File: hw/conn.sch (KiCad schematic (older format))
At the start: 8 parts

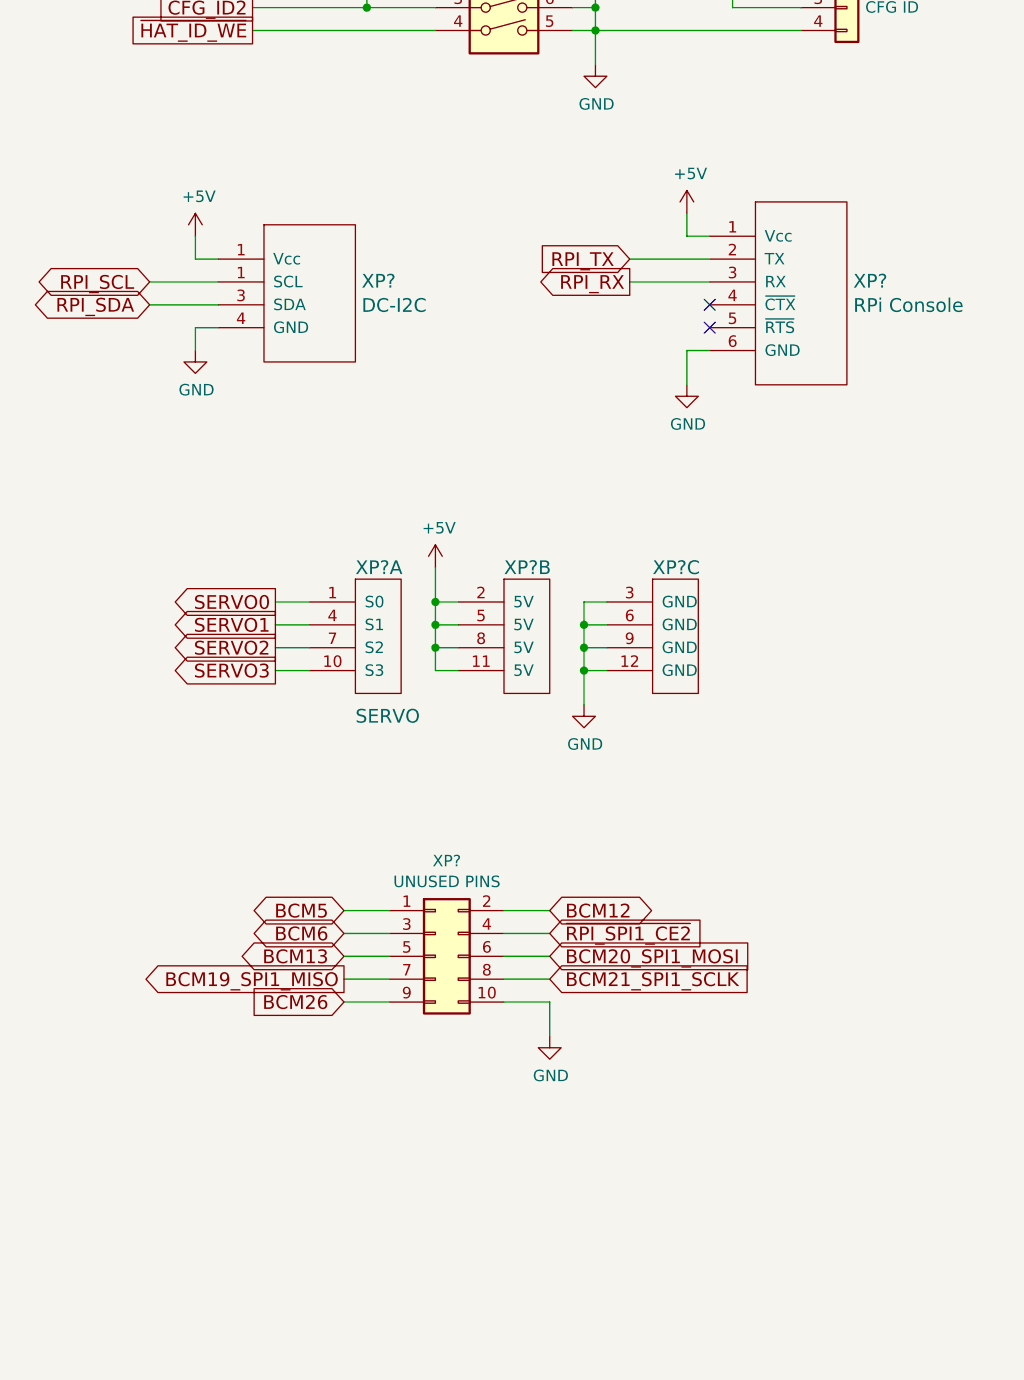
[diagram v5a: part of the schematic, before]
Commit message: hw: replace STM console and SWD with one connector. Rpi I2C and UART to DroneCode GPS port
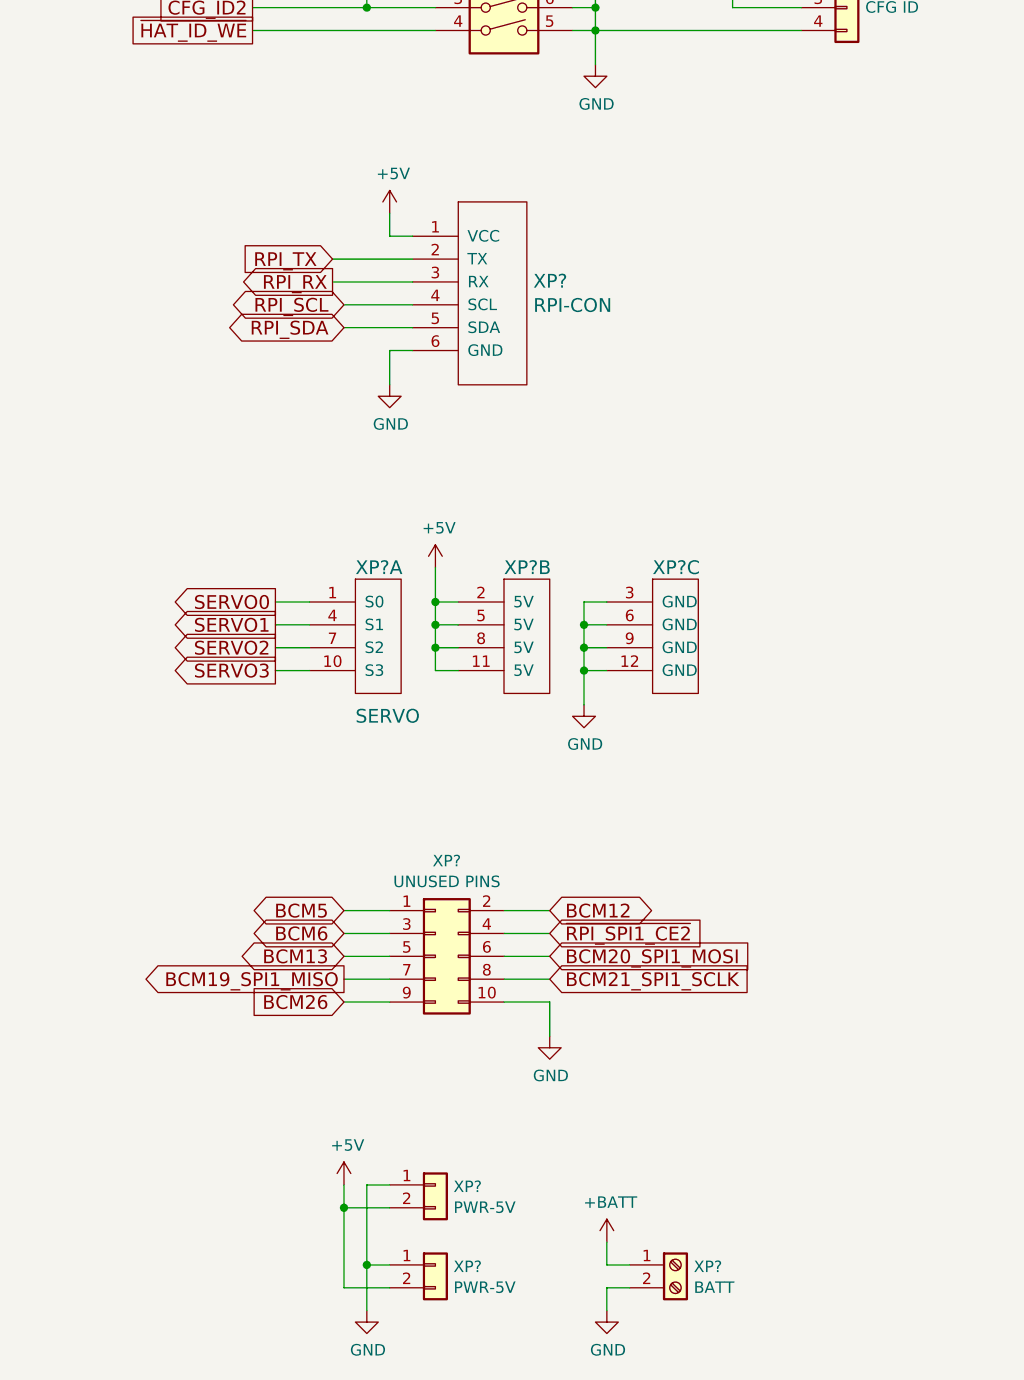
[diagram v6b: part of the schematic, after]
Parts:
- removed XP?: DC-I2C, symbol dronecode-conn:DC-I2C
- removed XP?: RPi Console, symbol dronecode-conn:DC-Telemetry
- added XP? (x2): PWR-5V, symbol Connector_Generic:Conn_01x02
- added XP?: BATT, symbol Connector_Specialized:Screw_Terminal_01x02
- added XP?: RPI-CON, symbol dronecode-conn:DC-GPS
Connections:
- net +5V: now also XP?.1 (VCC), XP?.2 (Pin_2), XP?.2 (Pin_2)
- net GND: now also XP?.1 (Pin_1), XP?.1 (Pin_1), XP?.2 (Pin_2), XP?.6 (GND)
- net RPI_RX: now also XP?.3 (RX)
- net RPI_SCL: now also XP?.4 (SCL)
- net RPI_SDA: now also XP?.5 (SDA)
- net RPI_TX: now also XP?.2 (TX)
- new net +BATT: XP?.1 (Pin_1)
- no-connect marks 2 -> 0
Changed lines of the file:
@@
 Wire Wire Line
 	3150 3150 3650 3150
-Text GLabel 4800 4250 0    60   Input ~ 0
+Text GLabel 3500 4250 0    60   Input ~ 0
 RPI_TX
-Text GLabel 4800 4350 0    60   Output ~ 0
+Text GLabel 3500 4350 0    60   Output ~ 0
 RPI_RX
 Text GLabel 4450 7300 2    60   Input ~ 0
@@
 Text GLabel 4450 7100 2    60   BiDi ~ 0
 BCM12
-Text GLabel 2700 4350 0    60   BiDi ~ 0
+Text GLabel 3550 4450 0    60   BiDi ~ 0
 RPI_SCL
-Text GLabel 2700 4450 0    60   BiDi ~ 0
+Text GLabel 3550 4550 0    60   BiDi ~ 0
 RPI_SDA
 Text GLabel 3550 7400 0    60   Output ~ 0
@@
 Text GLabel 3550 7200 0    60   BiDi ~ 0
 BCM6
-$Comp
-L dronecode-conn:DC-I2C XP?
-U 1 1 5AC44595
-P 3400 4400
-F 0 "XP?" H 3627 4453 60  0000 L CNN
-F 1 "DC-I2C" H 3627 4347 60  0000 L CNN
-F 2 "" H 3400 4400 60  0001 C CNN
-F 3 "https://wiki.dronecode.org/workgroup/connectors/start" H 3400 4400 60  0001 C CNN
-	1    3400 4400
-	1    0    0    -1
-$EndComp
-Wire Wire Line
-	2700 4350 3000 4350
-Wire Wire Line
-	2700 4450 3000 4450
-$Comp
-L power:GND #PWR?
-U 1 1 5AC44B9B
-P 2900 4650
-F 0 "#PWR?" H 2900 4400 50  0001 C CNN
-F 1 "GND" H 2905 4477 50  0000 C CNN
-F 2 "" H 2900 4650 50  0001 C CNN
-F 3 "" H 2900 4650 50  0001 C CNN
-	1    2900 4650
-	1    0    0    -1
-$EndComp
-$Comp
-L power:+5V #PWR?
-U 1 1 5AC44BF4
-P 2900 4150
-F 0 "#PWR?" H 2900 4000 50  0001 C CNN
-F 1 "+5V" H 2915 4323 50  0000 C CNN
-F 2 "" H 2900 4150 50  0001 C CNN
-F 3 "" H 2900 4150 50  0001 C CNN
-	1    2900 4150
-	1    0    0    -1
-$EndComp
-Wire Wire Line
-	3000 4250 2900 4250
-Wire Wire Line
-	2900 4250 2900 4150
-Wire Wire Line
-	2900 4650 2900 4550
-Wire Wire Line
-	2900 4550 3000 4550
+Wire Wire Line
+	3550 4450 3850 4450
+Wire Wire Line
+	3550 4550 3850 4550
 Text GLabel 3250 5750 0    60   Output ~ 0
 SERVO0
@@
 	5550 3250 4650 3250
 $Comp
-L dronecode-conn:DC-Telemetry XP?
-U 1 1 5AE1F895
-P 5550 4400
-F 0 "XP?" H 5778 4453 60  0000 L CNN
-F 1 "RPi Console" H 5778 4347 60  0000 L CNN
-F 2 "" H 5550 4400 60  0001 C CNN
-F 3 "https://wiki.dronecode.org/workgroup/connectors/start" H 5550 4400 60  0001 C CNN
-	1    5550 4400
-	1    0    0    -1
-$EndComp
-$Comp
 L power:GND #PWR?
 U 1 1 5AE1FA9F
-P 5050 4800
-F 0 "#PWR?" H 5050 4550 50  0001 C CNN
-F 1 "GND" H 5055 4627 50  0000 C CNN
-F 2 "" H 5050 4800 50  0001 C CNN
-F 3 "" H 5050 4800 50  0001 C CNN
-	1    5050 4800
+P 3750 4800
+F 0 "#PWR?" H 3750 4550 50  0001 C CNN
+F 1 "GND" H 3755 4627 50  0000 C CNN
+F 2 "" H 3750 4800 50  0001 C CNN
+F 3 "" H 3750 4800 50  0001 C CNN
+	1    3750 4800
 	1    0    0    -1
 $EndComp
@@
 L power:+5V #PWR?
 U 1 1 5AE1FAB8
-P 5050 4050
-F 0 "#PWR?" H 5050 3900 50  0001 C CNN
-F 1 "+5V" H 5065 4223 50  0000 C CNN
-F 2 "" H 5050 4050 50  0001 C CNN
-F 3 "" H 5050 4050 50  0001 C CNN
-	1    5050 4050
-	1    0    0    -1
-$EndComp
-Wire Wire Line
-	4800 4250 5150 4250
-Wire Wire Line
-	5150 4350 4800 4350
-Wire Wire Line
-	5150 4150 5050 4150
-Wire Wire Line
-	5050 4150 5050 4050
-Wire Wire Line
-	5150 4650 5050 4650
-Wire Wire Line
-	5050 4650 5050 4800
-NoConn ~ 5150 4550
-NoConn ~ 5150 4450
+P 3750 4050
+F 0 "#PWR?" H 3750 3900 50  0001 C CNN
+F 1 "+5V" H 3765 4223 50  0000 C CNN
+F 2 "" H 3750 4050 50  0001 C CNN
+F 3 "" H 3750 4050 50  0001 C CNN
+	1    3750 4050
+	1    0    0    -1
+$EndComp
+Wire Wire Line
+	3500 4250 3850 4250
+Wire Wire Line
+	3850 4350 3500 4350
+Wire Wire Line
+	3850 4150 3750 4150
+Wire Wire Line
+	3750 4150 3750 4050
+Wire Wire Line
+	3850 4650 3750 4650
+Wire Wire Line
+	3750 4650 3750 4800
 $Comp
 L Connector_Generic:Conn_02x05_Odd_Even XP?
@@
 Wire Wire Line
 	4450 7500 4450 7650
+$Comp
+L Connector_Generic:Conn_01x02 XP?
+U 1 1 5ADAC8B3
+P 3950 8300
+F 0 "XP?" H 4029 8292 50  0000 L CNN
+F 1 "PWR-5V" H 4029 8201 50  0000 L CNN
+F 2 "" H 3950 8300 50  0001 C CNN
+F 3 "~" H 3950 8300 50  0001 C CNN
+	1    3950 8300
+	1    0    0    -1
+$EndComp
+$Comp
+L Connector_Generic:Conn_01x02 XP?
+U 1 1 5ADACAD0
+P 3950 8650
+F 0 "XP?" H 4029 8642 50  0000 L CNN
+F 1 "PWR-5V" H 4029 8551 50  0000 L CNN
+F 2 "" H 3950 8650 50  0001 C CNN
+F 3 "~" H 3950 8650 50  0001 C CNN
+	1    3950 8650
+	1    0    0    -1
+$EndComp
+$Comp
+L power:GND #PWR?
+U 1 1 5ADAE6E2
+P 3650 8850
+F 0 "#PWR?" H 3650 8600 50  0001 C CNN
+F 1 "GND" H 3655 8677 50  0000 C CNN
+F 2 "" H 3650 8850 50  0001 C CNN
+F 3 "" H 3650 8850 50  0001 C CNN
+	1    3650 8850
+	1    0    0    -1
+$EndComp
+$Comp
+L power:+5V #PWR?
+U 1 1 5ADAEA7B
+P 3550 8300
+F 0 "#PWR?" H 3550 8150 50  0001 C CNN
+F 1 "+5V" H 3565 8473 50  0000 C CNN
+F 2 "" H 3550 8300 50  0001 C CNN
+F 3 "" H 3550 8300 50  0001 C CNN
+	1    3550 8300
+	1    0    0    -1
+$EndComp
+Wire Wire Line
+	3750 8300 3650 8300
+Wire Wire Line
+	3650 8300 3650 8650
+Wire Wire Line
+	3650 8650 3750 8650
+Connection ~ 3650 8650
+Wire Wire Line
+	3650 8650 3650 8850
+Wire Wire Line
+	3750 8750 3550 8750
+Wire Wire Line
+	3550 8750 3550 8400
+Wire Wire Line
+	3750 8400 3550 8400
+Connection ~ 3550 8400
+Wire Wire Line
+	3550 8400 3550 8300
+$Comp
+L Connector_Specialized:Screw_Terminal_01x02 XP?
+U 1 1 5ADC296E
+P 5000 8650
+F 0 "XP?" H 5080 8642 50  0000 L CNN
+F 1 "BATT" H 5080 8551 50  0000 L CNN
+F 2 "" H 5000 8650 50  0001 C CNN
+F 3 "~" H 5000 8650 50  0001 C CNN
+	1    5000 8650
+	1    0    0    -1
+$EndComp
+$Comp
+L power:GND #PWR?
+U 1 1 5ADC2D33
+P 4700 8850
+F 0 "#PWR?" H 4700 8600 50  0001 C CNN
+F 1 "GND" H 4705 8677 50  0000 C CNN
+F 2 "" H 4700 8850 50  0001 C CNN
+F 3 "" H 4700 8850 50  0001 C CNN
+	1    4700 8850
+	1    0    0    -1
+$EndComp
+$Comp
+L power:+BATT #PWR?
+U 1 1 5ADC2DB8
+P 4700 8550
+F 0 "#PWR?" H 4700 8400 50  0001 C CNN
+F 1 "+BATT" H 4715 8723 50  0000 C CNN
+F 2 "" H 4700 8550 50  0001 C CNN
+F 3 "" H 4700 8550 50  0001 C CNN
+	1    4700 8550
+	1    0    0    -1
+$EndComp
+Wire Wire Line
+	4800 8650 4700 8650
+Wire Wire Line
+	4700 8650 4700 8550
+Wire Wire Line
+	4800 8750 4700 8750
+Wire Wire Line
+	4700 8750 4700 8850
+$Comp
+L dronecode-conn:DC-GPS XP?
+U 1 1 5AE4627A
+P 4200 4400
+F 0 "XP?" H 4378 4453 60  0000 L CNN
+F 1 "RPI-CON" H 4378 4347 60  0000 L CNN
+F 2 "" H 4150 4400 60  0001 C CNN
+F 3 "" H 4150 4400 60  0001 C CNN
+	1    4200 4400
+	1    0    0    -1
+$EndComp
 $EndSCHEMATC

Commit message: hw: sch ready
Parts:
- gave numbers to parts that had none: 9
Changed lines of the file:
@@
 $EndDescr
 $Comp
-L Switch:SW_DIP_x04 SW?
+L Switch:SW_DIP_x04 SW1
 U 1 1 5AC0CE65
 P 4250 3150
-F 0 "SW?" H 4250 3617 50  0000 C CNN
+F 0 "SW1" H 4250 3617 50  0000 C CNN
 F 1 "SW_DIP_x04" H 4250 3526 50  0000 C CNN
 F 2 "" H 4250 3150 50  0001 C CNN
@@
 	3150 3050 3550 3050
 $Comp
-L power:GND #PWR?
+L power:GND #PWR049
 U 1 1 5AC0D0C3
 P 4650 3400
-F 0 "#PWR?" H 4650 3150 50  0001 C CNN
+F 0 "#PWR049" H 4650 3150 50  0001 C CNN
 F 1 "GND" H 4655 3227 50  0000 C CNN
 F 2 "" H 4650 3400 50  0001 C CNN
@@
 SERVO3
 $Comp
-L dronecode-conn:Servo-Conn4 XP?
+L dronecode-conn:Servo-Conn4 XP10
 U 1 1 5AE13059
 P 3700 5900
-F 0 "XP?" H 3600 6200 60  0000 L CNN
+F 0 "XP10" H 3600 6200 60  0000 L CNN
 F 1 "SERVO" H 3600 5550 60  0000 L CNN
 F 2 "" H 3650 5900 60  0001 C CNN
@@
 $EndComp
 $Comp
-L dronecode-conn:Servo-Conn4 XP?
+L dronecode-conn:Servo-Conn4 XP11
 U 2 1 5AE130D9
 P 4350 5900
-F 0 "XP?" H 4250 6200 60  0000 L CNN
+F 0 "XP11" H 4250 6200 60  0000 L CNN
 F 1 "Servo-Conn4" H 4477 5847 60  0001 L CNN
 F 2 "" H 4300 5900 60  0001 C CNN
@@
 $EndComp
 $Comp
-L dronecode-conn:Servo-Conn4 XP?
+L dronecode-conn:Servo-Conn4 XP11
 U 3 1 5AE13114
 P 5000 5900
-F 0 "XP?" H 4900 6200 60  0000 L CNN
+F 0 "XP11" H 4900 6200 60  0000 L CNN
 F 1 "Servo-Conn4" H 5127 5847 60  0001 L CNN
 F 2 "" H 4950 5900 60  0001 C CNN
@@
 	3250 6050 3400 6050
 $Comp
-L power:GND #PWR?
+L power:GND #PWR053
 U 1 1 5AE14A11
 P 4600 6200
-F 0 "#PWR?" H 4600 5950 50  0001 C CNN
+F 0 "#PWR053" H 4600 5950 50  0001 C CNN
 F 1 "GND" H 4605 6027 50  0000 C CNN
 F 2 "" H 4600 6200 50  0001 C CNN
@@
 $EndComp
 $Comp
-L power:+5V #PWR?
+L power:+5V #PWR052
 U 1 1 5AE14A3F
 P 3950 5600
-F 0 "#PWR?" H 3950 5450 50  0001 C CNN
+F 0 "#PWR052" H 3950 5450 50  0001 C CNN
 F 1 "+5V" H 3965 5773 50  0000 C CNN
 F 2 "" H 3950 5600 50  0001 C CNN
@@
 	4600 6050 4600 6200
 $Comp
-L Connector_Generic:Conn_01x04 XP?
+L Connector_Generic:Conn_01x04 XP8
 U 1 1 5AE192BA
 P 5750 3050
-F 0 "XP?" H 5830 3042 50  0000 L CNN
+F 0 "XP8" H 5830 3042 50  0000 L CNN
 F 1 "CFG ID" H 5830 2951 50  0000 L CNN
 F 2 "" H 5750 3050 50  0001 C CNN
@@
 	5550 3250 4650 3250
 $Comp
-L power:GND #PWR?
+L power:GND #PWR051
 U 1 1 5AE1FA9F
 P 3750 4800
-F 0 "#PWR?" H 3750 4550 50  0001 C CNN
+F 0 "#PWR051" H 3750 4550 50  0001 C CNN
 F 1 "GND" H 3755 4627 50  0000 C CNN
 F 2 "" H 3750 4800 50  0001 C CNN
@@
 $EndComp
 $Comp
-L power:+5V #PWR?
+L power:+5V #PWR050
 U 1 1 5AE1FAB8
 P 3750 4050
-F 0 "#PWR?" H 3750 3900 50  0001 C CNN
+F 0 "#PWR050" H 3750 3900 50  0001 C CNN
 F 1 "+5V" H 3765 4223 50  0000 C CNN
 F 2 "" H 3750 4050 50  0001 C CNN
@@
 	3750 4650 3750 4800
 $Comp
-L Connector_Generic:Conn_02x05_Odd_Even XP?
+L Connector_Generic:Conn_02x05_Odd_Even XP12
 U 1 1 5AE27376
 P 3950 7300
-F 0 "XP?" H 4000 7717 50  0000 C CNN
+F 0 "XP12" H 4000 7717 50  0000 C CNN
 F 1 "UNUSED PINS" H 4000 7626 50  0000 C CNN
 F 2 "" H 3950 7300 50  0001 C CNN
@@
 $EndComp
 $Comp
-L power:GND #PWR?
+L power:GND #PWR054
 U 1 1 5AE2781B
 P 4450 7650
-F 0 "#PWR?" H 4450 7400 50  0001 C CNN
+F 0 "#PWR054" H 4450 7400 50  0001 C CNN
 F 1 "GND" H 4455 7477 50  0000 C CNN
 F 2 "" H 4450 7650 50  0001 C CNN
@@
 	4450 7500 4450 7650
 $Comp
-L Connector_Generic:Conn_01x02 XP?
+L Connector_Generic:Conn_01x02 XP13
 U 1 1 5ADAC8B3
 P 3950 8300
-F 0 "XP?" H 4029 8292 50  0000 L CNN
+F 0 "XP13" H 4029 8292 50  0000 L CNN
 F 1 "PWR-5V" H 4029 8201 50  0000 L CNN
 F 2 "" H 3950 8300 50  0001 C CNN
@@
 $EndComp
 $Comp
-L Connector_Generic:Conn_01x02 XP?
+L Connector_Generic:Conn_01x02 XP14
 U 1 1 5ADACAD0
 P 3950 8650
-F 0 "XP?" H 4029 8642 50  0000 L CNN
+F 0 "XP14" H 4029 8642 50  0000 L CNN
 F 1 "PWR-5V" H 4029 8551 50  0000 L CNN
 F 2 "" H 3950 8650 50  0001 C CNN
@@
 $EndComp
 $Comp
-L power:GND #PWR?
+L power:GND #PWR057
 U 1 1 5ADAE6E2
 P 3650 8850
-F 0 "#PWR?" H 3650 8600 50  0001 C CNN
+F 0 "#PWR057" H 3650 8600 50  0001 C CNN
 F 1 "GND" H 3655 8677 50  0000 C CNN
 F 2 "" H 3650 8850 50  0001 C CNN
@@
 $EndComp
 $Comp
-L power:+5V #PWR?
+L power:+5V #PWR055
 U 1 1 5ADAEA7B
 P 3550 8300
-F 0 "#PWR?" H 3550 8150 50  0001 C CNN
+F 0 "#PWR055" H 3550 8150 50  0001 C CNN
 F 1 "+5V" H 3565 8473 50  0000 C CNN
 F 2 "" H 3550 8300 50  0001 C CNN
@@
 	3550 8400 3550 8300
 $Comp
-L Connector_Specialized:Screw_Terminal_01x02 XP?
+L Connector_Specialized:Screw_Terminal_01x02 XP15
 U 1 1 5ADC296E
 P 5000 8650
-F 0 "XP?" H 5080 8642 50  0000 L CNN
+F 0 "XP15" H 5080 8642 50  0000 L CNN
 F 1 "BATT" H 5080 8551 50  0000 L CNN
 F 2 "" H 5000 8650 50  0001 C CNN
@@
 $EndComp
 $Comp
-L power:GND #PWR?
+L power:GND #PWR058
 U 1 1 5ADC2D33
 P 4700 8850
-F 0 "#PWR?" H 4700 8600 50  0001 C CNN
+F 0 "#PWR058" H 4700 8600 50  0001 C CNN
 F 1 "GND" H 4705 8677 50  0000 C CNN
 F 2 "" H 4700 8850 50  0001 C CNN
@@
 $EndComp
 $Comp
-L power:+BATT #PWR?
+L power:+BATT #PWR056
 U 1 1 5ADC2DB8
 P 4700 8550
-F 0 "#PWR?" H 4700 8400 50  0001 C CNN
+F 0 "#PWR056" H 4700 8400 50  0001 C CNN
 F 1 "+BATT" H 4715 8723 50  0000 C CNN
 F 2 "" H 4700 8550 50  0001 C CNN
@@
 	4700 8750 4700 8850
 $Comp
-L dronecode-conn:DC-GPS XP?
+L dronecode-conn:DC-GPS XP9
 U 1 1 5AE4627A
 P 4200 4400
-F 0 "XP?" H 4378 4453 60  0000 L CNN
+F 0 "XP9" H 4378 4453 60  0000 L CNN
 F 1 "RPI-CON" H 4378 4347 60  0000 L CNN
 F 2 "" H 4150 4400 60  0001 C CNN

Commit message: hw: more cvpcb
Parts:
- SW1: footprint (none) -> Button_Switch_THT:SW_DIP_SPSTx04_Slide_9.78x12.34mm_W7.62mm_P2.54mm
- XP10: renamed from XP11; value Servo-Conn4 -> SERVO
- XP11: renamed from XP12; footprint (none) -> Connector_PinSocket_2.00mm:PinSocket_2x05_P2.00mm_Vertical
- XP12: renamed from XP13; footprint (none) -> Connector_JST:JST_PH_B2B-PH-K_1x02_P2.00mm_Vertical
- XP13: renamed from XP14; footprint (none) -> Connector_JST:JST_PH_B2B-PH-K_1x02_P2.00mm_Vertical
- XP8: footprint (none) -> Connector_JST:JST_PH_B4B-PH-K_1x04_P2.00mm_Vertical
- XP9: footprint (none) -> Connector_JST:JST_GH_BM06B-GHS-TBT_1x06-1MP_P1.25mm_Vertical
- renumbered XP15 to XP14
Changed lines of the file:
@@
 F 0 "SW1" H 4250 3617 50  0000 C CNN
 F 1 "SW_DIP_x04" H 4250 3526 50  0000 C CNN
-F 2 "" H 4250 3150 50  0001 C CNN
+F 2 "Button_Switch_THT:SW_DIP_SPSTx04_Slide_9.78x12.34mm_W7.62mm_P2.54mm" H 4250 3150 50  0001 C CNN
 F 3 "" H 4250 3150 50  0001 C CNN
 	1    4250 3150
@@
 $EndComp
 $Comp
-L dronecode-conn:Servo-Conn4 XP11
+L dronecode-conn:Servo-Conn4 XP10
 U 2 1 5AE130D9
 P 4350 5900
-F 0 "XP11" H 4250 6200 60  0000 L CNN
-F 1 "Servo-Conn4" H 4477 5847 60  0001 L CNN
+F 0 "XP10" H 4250 6200 60  0000 L CNN
+F 1 "SERVO" H 4477 5847 60  0001 L CNN
 F 2 "" H 4300 5900 60  0001 C CNN
 F 3 "" H 4300 5900 60  0001 C CNN
@@
 $EndComp
 $Comp
-L dronecode-conn:Servo-Conn4 XP11
+L dronecode-conn:Servo-Conn4 XP10
 U 3 1 5AE13114
 P 5000 5900
-F 0 "XP11" H 4900 6200 60  0000 L CNN
-F 1 "Servo-Conn4" H 5127 5847 60  0001 L CNN
+F 0 "XP10" H 4900 6200 60  0000 L CNN
+F 1 "SERVO" H 5127 5847 60  0001 L CNN
 F 2 "" H 4950 5900 60  0001 C CNN
 F 3 "" H 4950 5900 60  0001 C CNN
@@
 F 0 "XP8" H 5830 3042 50  0000 L CNN
 F 1 "CFG ID" H 5830 2951 50  0000 L CNN
-F 2 "" H 5750 3050 50  0001 C CNN
+F 2 "Connector_JST:JST_PH_B4B-PH-K_1x04_P2.00mm_Vertical" H 5750 3050 50  0001 C CNN
 F 3 "~" H 5750 3050 50  0001 C CNN
 	1    5750 3050
@@
 	3750 4650 3750 4800
 $Comp
-L Connector_Generic:Conn_02x05_Odd_Even XP12
+L Connector_Generic:Conn_02x05_Odd_Even XP11
 U 1 1 5AE27376
 P 3950 7300
-F 0 "XP12" H 4000 7717 50  0000 C CNN
+F 0 "XP11" H 4000 7717 50  0000 C CNN
 F 1 "UNUSED PINS" H 4000 7626 50  0000 C CNN
-F 2 "" H 3950 7300 50  0001 C CNN
+F 2 "Connector_PinSocket_2.00mm:PinSocket_2x05_P2.00mm_Vertical" H 3950 7300 50  0001 C CNN
 F 3 "~" H 3950 7300 50  0001 C CNN
 	1    3950 7300
@@
 	4450 7500 4450 7650
 $Comp
-L Connector_Generic:Conn_01x02 XP13
+L Connector_Generic:Conn_01x02 XP12
 U 1 1 5ADAC8B3
 P 3950 8300
-F 0 "XP13" H 4029 8292 50  0000 L CNN
+F 0 "XP12" H 4029 8292 50  0000 L CNN
 F 1 "PWR-5V" H 4029 8201 50  0000 L CNN
-F 2 "" H 3950 8300 50  0001 C CNN
+F 2 "Connector_JST:JST_PH_B2B-PH-K_1x02_P2.00mm_Vertical" H 3950 8300 50  0001 C CNN
 F 3 "~" H 3950 8300 50  0001 C CNN
 	1    3950 8300
@@
 $EndComp
 $Comp
-L Connector_Generic:Conn_01x02 XP14
+L Connector_Generic:Conn_01x02 XP13
 U 1 1 5ADACAD0
 P 3950 8650
-F 0 "XP14" H 4029 8642 50  0000 L CNN
+F 0 "XP13" H 4029 8642 50  0000 L CNN
 F 1 "PWR-5V" H 4029 8551 50  0000 L CNN
-F 2 "" H 3950 8650 50  0001 C CNN
+F 2 "Connector_JST:JST_PH_B2B-PH-K_1x02_P2.00mm_Vertical" H 3950 8650 50  0001 C CNN
 F 3 "~" H 3950 8650 50  0001 C CNN
 	1    3950 8650
@@
 	3550 8400 3550 8300
 $Comp
-L Connector_Specialized:Screw_Terminal_01x02 XP15
+L Connector_Specialized:Screw_Terminal_01x02 XP14
 U 1 1 5ADC296E
 P 5000 8650
-F 0 "XP15" H 5080 8642 50  0000 L CNN
+F 0 "XP14" H 5080 8642 50  0000 L CNN
 F 1 "BATT" H 5080 8551 50  0000 L CNN
 F 2 "" H 5000 8650 50  0001 C CNN
@@
 F 0 "XP9" H 4378 4453 60  0000 L CNN
 F 1 "RPI-CON" H 4378 4347 60  0000 L CNN
-F 2 "" H 4150 4400 60  0001 C CNN
+F 2 "Connector_JST:JST_GH_BM06B-GHS-TBT_1x06-1MP_P1.25mm_Vertical" H 4150 4400 60  0001 C CNN
 F 3 "" H 4150 4400 60  0001 C CNN
 	1    4200 4400
